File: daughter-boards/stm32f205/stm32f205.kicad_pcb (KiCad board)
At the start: 2 copper layers, 33 x 91.4 mm, 50 parts, among them J1 Conn_02x10_Odd_Even, J2 Conn_02x10_Odd_Even, U1 STM32F205RETx, Y1 Crystal_Small

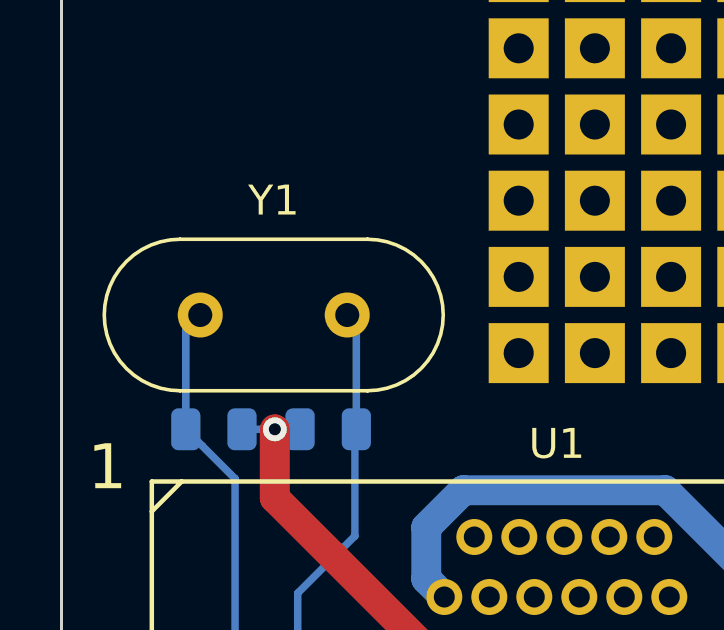
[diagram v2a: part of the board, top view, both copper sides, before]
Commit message: fix(daugtherboard): update the schematics after modification of STM32 symbol from Kicad update
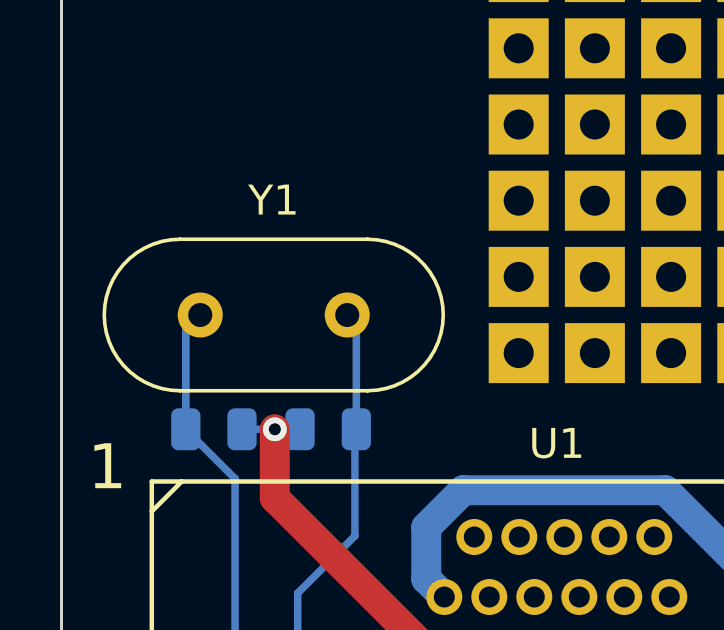
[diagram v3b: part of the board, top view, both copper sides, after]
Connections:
- J1 pad 10: Net-(J1-Pad10) -> unconnected-(J1-Pin_10-Pad10)
- J1 pad 11: Net-(J1-Pad11) -> unconnected-(J1-Pin_11-Pad11)
- J1 pad 12: Net-(J1-Pad12) -> unconnected-(J1-Pin_12-Pad12)
- J1 pad 13: Net-(J1-Pad13) -> unconnected-(J1-Pin_13-Pad13)
- J1 pad 14: Net-(J1-Pad14) -> unconnected-(J1-Pin_14-Pad14)
- J1 pad 15: Net-(J1-Pad15) -> unconnected-(J1-Pin_15-Pad15)
- J1 pad 16: Net-(J1-Pad16) -> unconnected-(J1-Pin_16-Pad16)
- J1 pad 18: Net-(J1-Pad18) -> unconnected-(J1-Pin_18-Pad18)
- J1 pad 5: Net-(J1-Pad5) -> unconnected-(J1-Pin_5-Pad5)
- J1 pad 6: Net-(J1-Pad6) -> unconnected-(J1-Pin_6-Pad6)
- J1 pad 9: Net-(J1-Pad9) -> unconnected-(J1-Pin_9-Pad9)
- J2 pad 1: Net-(J2-Pad1) -> unconnected-(J2-Pin_1-Pad1)
- J2 pad 10: Net-(J2-Pad10) -> unconnected-(J2-Pin_10-Pad10)
- J2 pad 11: Net-(J2-Pad11) -> unconnected-(J2-Pin_11-Pad11)
- J2 pad 12: Net-(J2-Pad12) -> unconnected-(J2-Pin_12-Pad12)
- J2 pad 13: Net-(J2-Pad13) -> unconnected-(J2-Pin_13-Pad13)
- J2 pad 14: Net-(J2-Pad14) -> unconnected-(J2-Pin_14-Pad14)
- J2 pad 15: Net-(J2-Pad15) -> unconnected-(J2-Pin_15-Pad15)
- J2 pad 16: Net-(J2-Pad16) -> unconnected-(J2-Pin_16-Pad16)
- J2 pad 17: Net-(J2-Pad17) -> unconnected-(J2-Pin_17-Pad17)
- J2 pad 18: Net-(J2-Pad18) -> unconnected-(J2-Pin_18-Pad18)
- J2 pad 19: Net-(J2-Pad19) -> unconnected-(J2-Pin_19-Pad19)
- J2 pad 2: Net-(J2-Pad2) -> unconnected-(J2-Pin_2-Pad2)
- J2 pad 20: Net-(J2-Pad20) -> unconnected-(J2-Pin_20-Pad20)
- J2 pad 3: Net-(J2-Pad3) -> unconnected-(J2-Pin_3-Pad3)
- J2 pad 4: Net-(J2-Pad4) -> unconnected-(J2-Pin_4-Pad4)
- J2 pad 5: Net-(J2-Pad5) -> unconnected-(J2-Pin_5-Pad5)
- J2 pad 6: Net-(J2-Pad6) -> unconnected-(J2-Pin_6-Pad6)
- J2 pad 7: Net-(J2-Pad7) -> unconnected-(J2-Pin_7-Pad7)
- J2 pad 8: Net-(J2-Pad8) -> unconnected-(J2-Pin_8-Pad8)
- J2 pad 9: Net-(J2-Pad9) -> unconnected-(J2-Pin_9-Pad9)
- TP1 pad 1: Net-(TP1-Pad1) -> unconnected-(TP1-Pad1)
- TP10 pad 1: Net-(TP10-Pad1) -> unconnected-(TP10-Pad1)
- TP11 pad 1: Net-(TP11-Pad1) -> unconnected-(TP11-Pad1)
- TP12 pad 1: Net-(TP12-Pad1) -> unconnected-(TP12-Pad1)
- TP13 pad 1: Net-(TP13-Pad1) -> unconnected-(TP13-Pad1)
- TP14 pad 1: Net-(TP14-Pad1) -> unconnected-(TP14-Pad1)
- TP15 pad 1: Net-(TP15-Pad1) -> unconnected-(TP15-Pad1)
- TP16 pad 1: Net-(TP16-Pad1) -> unconnected-(TP16-Pad1)
- TP17 pad 1: Net-(TP17-Pad1) -> unconnected-(TP17-Pad1)
- TP18 pad 1: Net-(TP18-Pad1) -> unconnected-(TP18-Pad1)
- TP19 pad 1: Net-(TP19-Pad1) -> unconnected-(TP19-Pad1)
- TP2 pad 1: Net-(TP2-Pad1) -> unconnected-(TP2-Pad1)
- TP20 pad 1: Net-(TP20-Pad1) -> unconnected-(TP20-Pad1)
- TP21 pad 1: Net-(TP21-Pad1) -> unconnected-(TP21-Pad1)
- TP22 pad 1: Net-(TP22-Pad1) -> unconnected-(TP22-Pad1)
- TP23 pad 1: Net-(TP23-Pad1) -> unconnected-(TP23-Pad1)
- TP24 pad 1: Net-(TP24-Pad1) -> unconnected-(TP24-Pad1)
- TP25 pad 1: Net-(TP25-Pad1) -> unconnected-(TP25-Pad1)
- TP26 pad 1: Net-(TP26-Pad1) -> unconnected-(TP26-Pad1)
- TP27 pad 1: Net-(TP27-Pad1) -> unconnected-(TP27-Pad1)
- TP28 pad 1: Net-(TP28-Pad1) -> unconnected-(TP28-Pad1)
- TP29 pad 1: Net-(TP29-Pad1) -> unconnected-(TP29-Pad1)
- TP3 pad 1: Net-(TP3-Pad1) -> unconnected-(TP3-Pad1)
- TP30 pad 1: Net-(TP30-Pad1) -> unconnected-(TP30-Pad1)
- TP31 pad 1: Net-(TP31-Pad1) -> unconnected-(TP31-Pad1)
- TP32 pad 1: Net-(TP32-Pad1) -> unconnected-(TP32-Pad1)
- TP33 pad 1: Net-(TP33-Pad1) -> unconnected-(TP33-Pad1)
- TP34 pad 1: Net-(TP34-Pad1) -> unconnected-(TP34-Pad1)
- TP35 pad 1: Net-(TP35-Pad1) -> unconnected-(TP35-Pad1)
- TP36 pad 1: Net-(TP36-Pad1) -> unconnected-(TP36-Pad1)
- TP37 pad 1: Net-(TP37-Pad1) -> unconnected-(TP37-Pad1)
- TP38 pad 1: Net-(TP38-Pad1) -> unconnected-(TP38-Pad1)
- TP39 pad 1: Net-(TP39-Pad1) -> unconnected-(TP39-Pad1)
- TP4 pad 1: Net-(TP4-Pad1) -> unconnected-(TP4-Pad1)
- TP40 pad 1: Net-(TP40-Pad1) -> unconnected-(TP40-Pad1)
- TP41 pad 1: Net-(TP41-Pad1) -> unconnected-(TP41-Pad1)
- TP42 pad 1: Net-(TP42-Pad1) -> unconnected-(TP42-Pad1)
- TP5 pad 1: Net-(TP5-Pad1) -> unconnected-(TP5-Pad1)
- TP6 pad 1: Net-(TP6-Pad1) -> unconnected-(TP6-Pad1)
- TP7 pad 1: Net-(TP7-Pad1) -> unconnected-(TP7-Pad1)
- TP8 pad 1: Net-(TP8-Pad1) -> unconnected-(TP8-Pad1)
- TP9 pad 1: Net-(TP9-Pad1) -> unconnected-(TP9-Pad1)
- U1 pad 1: Net-(U1-Pad1) -> unconnected-(U1-VBAT-Pad1)
- U1 pad 10: Net-(U1-Pad10) -> unconnected-(U1-PC2-Pad10)
- U1 pad 11: Net-(U1-Pad11) -> unconnected-(U1-PC3-Pad11)
- U1 pad 14: Net-(U1-Pad14) -> unconnected-(U1-PA0-Pad14)
- U1 pad 15: Net-(U1-Pad15) -> unconnected-(U1-PA1-Pad15)
- U1 pad 16: Net-(U1-Pad16) -> unconnected-(U1-PA2-Pad16)
- U1 pad 17: Net-(U1-Pad17) -> unconnected-(U1-PA3-Pad17)
- U1 pad 2: Net-(U1-Pad2) -> unconnected-(U1-PC13-Pad2)
- U1 pad 20: Net-(U1-Pad20) -> unconnected-(U1-PA4-Pad20)
- U1 pad 21: Net-(U1-Pad21) -> unconnected-(U1-PA5-Pad21)
- U1 pad 22: Net-(U1-Pad22) -> unconnected-(U1-PA6-Pad22)
- U1 pad 23: Net-(U1-Pad23) -> unconnected-(U1-PA7-Pad23)
- U1 pad 24: Net-(U1-Pad24) -> unconnected-(U1-PC4-Pad24)
- U1 pad 25: Net-(U1-Pad25) -> unconnected-(U1-PC5-Pad25)
- U1 pad 26: Net-(U1-Pad26) -> unconnected-(U1-PB0-Pad26)
- U1 pad 27: Net-(U1-Pad27) -> unconnected-(U1-PB1-Pad27)
- U1 pad 29: Net-(U1-Pad29) -> unconnected-(U1-PB10-Pad29)
- U1 pad 3: Net-(U1-Pad3) -> unconnected-(U1-PC14-Pad3)
- U1 pad 30: Net-(U1-Pad30) -> unconnected-(U1-PB11-Pad30)
- U1 pad 31: Net-(U1-Pad31) -> unconnected-(U1-VCAP_1-Pad31)
- U1 pad 33: Net-(U1-Pad33) -> unconnected-(U1-PB12-Pad33)
- U1 pad 34: Net-(U1-Pad34) -> unconnected-(U1-PB13-Pad34)
- U1 pad 35: Net-(U1-Pad35) -> unconnected-(U1-PB14-Pad35)
- U1 pad 36: Net-(U1-Pad36) -> unconnected-(U1-PB15-Pad36)
- U1 pad 37: Net-(U1-Pad37) -> unconnected-(U1-PC6-Pad37)
- U1 pad 38: Net-(U1-Pad38) -> unconnected-(U1-PC7-Pad38)
- U1 pad 39: Net-(U1-Pad39) -> unconnected-(U1-PC8-Pad39)
- U1 pad 4: Net-(U1-Pad4) -> unconnected-(U1-PC15-Pad4)
- U1 pad 40: Net-(U1-Pad40) -> unconnected-(U1-PC9-Pad40)
- U1 pad 41: Net-(U1-Pad41) -> unconnected-(U1-PA8-Pad41)
- U1 pad 44: Net-(U1-Pad44) -> unconnected-(U1-PA11-Pad44)
- U1 pad 45: Net-(U1-Pad45) -> unconnected-(U1-PA12-Pad45)
- U1 pad 46: Net-(U1-Pad46) -> unconnected-(U1-PA13-Pad46)
- U1 pad 47: Net-(U1-Pad47) -> unconnected-(U1-VCAP_2-Pad47)
- U1 pad 49: Net-(U1-Pad49) -> unconnected-(U1-PA14-Pad49)
- U1 pad 50: Net-(U1-Pad50) -> unconnected-(U1-PA15-Pad50)
- U1 pad 51: Net-(U1-Pad51) -> unconnected-(U1-PC10-Pad51)
- U1 pad 52: Net-(U1-Pad52) -> unconnected-(U1-PC11-Pad52)
- U1 pad 53: Net-(U1-Pad53) -> unconnected-(U1-PC12-Pad53)
- U1 pad 54: Net-(U1-Pad54) -> unconnected-(U1-PD2-Pad54)
- U1 pad 55: Net-(U1-Pad55) -> unconnected-(U1-PB3-Pad55)
- U1 pad 56: Net-(U1-Pad56) -> unconnected-(U1-PB4-Pad56)
- U1 pad 57: Net-(U1-Pad57) -> unconnected-(U1-PB5-Pad57)
- U1 pad 58: Net-(U1-Pad58) -> unconnected-(U1-PB6-Pad58)
- U1 pad 59: Net-(U1-Pad59) -> unconnected-(U1-PB7-Pad59)
- U1 pad 61: Net-(U1-Pad61) -> unconnected-(U1-PB8-Pad61)
- U1 pad 62: Net-(U1-Pad62) -> unconnected-(U1-PB9-Pad62)
- U1 pad 9: Net-(U1-Pad9) -> unconnected-(U1-PC1-Pad9)
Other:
- net class Default removed
